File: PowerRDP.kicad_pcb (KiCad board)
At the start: 2 copper layers, 41.3 x 33.7 mm, 17 parts, among them J1 Conn_01x02_Male, J2 Conn_01x02_Male, J3 Conn_01x02_Male, J4 Conn_01x02_Male, J5 Conn_01x02_Male, J6 Conn_01x02_Male, J7 Conn_01x02_Male, J8 Conn_01x02_Male, J9 Conn_01x03_Male, U1 DPBW06F, U2 KA378R12C, U3 AZ1117-3.3

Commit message: Add pole descriptions on bottom silkscreen of +/-15V output
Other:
- board text added: "+"
- board text added: "-"
- board text added: "G"
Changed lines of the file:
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@@
   (general
     (thickness 1.6)
-    (drawings 16)
+    (drawings 19)
     (tracks 36)
     (zones 0)
@@
     (34 B.Paste user)
     (35 F.Paste user)
-    (36 B.SilkS user hide)
+    (36 B.SilkS user)
     (37 F.SilkS user)
     (38 B.Mask user)
-    (39 F.Mask user hide)
+    (39 F.Mask user)
     (40 Dwgs.User user)
     (41 Cmts.User user)
@@
       (xy -0.000377 -2.299489) (xy 0.01309 -2.299294)) (layer F.SilkS) (width 0.01))
   )
+  (gr_text - (at 159.766 63.754) (layer B.SilkS)
+    (effects (font (size 1 1) (thickness 0.2)) (justify mirror))
+  )
+  (gr_text + (at 157.226 63.754) (layer B.SilkS)
+    (effects (font (size 1 1) (thickness 0.2)) (justify mirror))
+  )
+  (gr_text G (at 154.432 63.754) (layer B.SilkS)
+    (effects (font (size 1 1) (thickness 0.2)) (justify mirror))
+  )
   (dimension 10.795 (width 0.3) (layer Eco1.User)

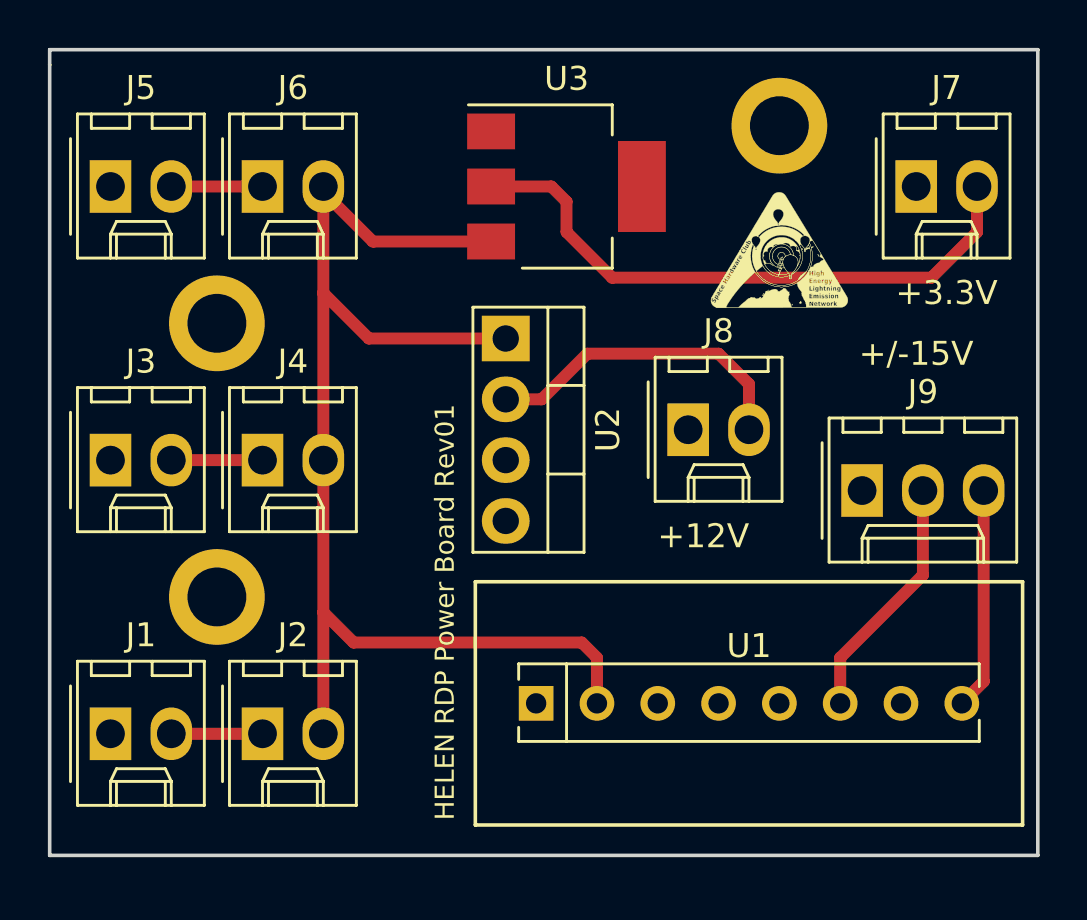
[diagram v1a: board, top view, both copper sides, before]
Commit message: Add power filtering to all regulators, correct +/-15V regulator
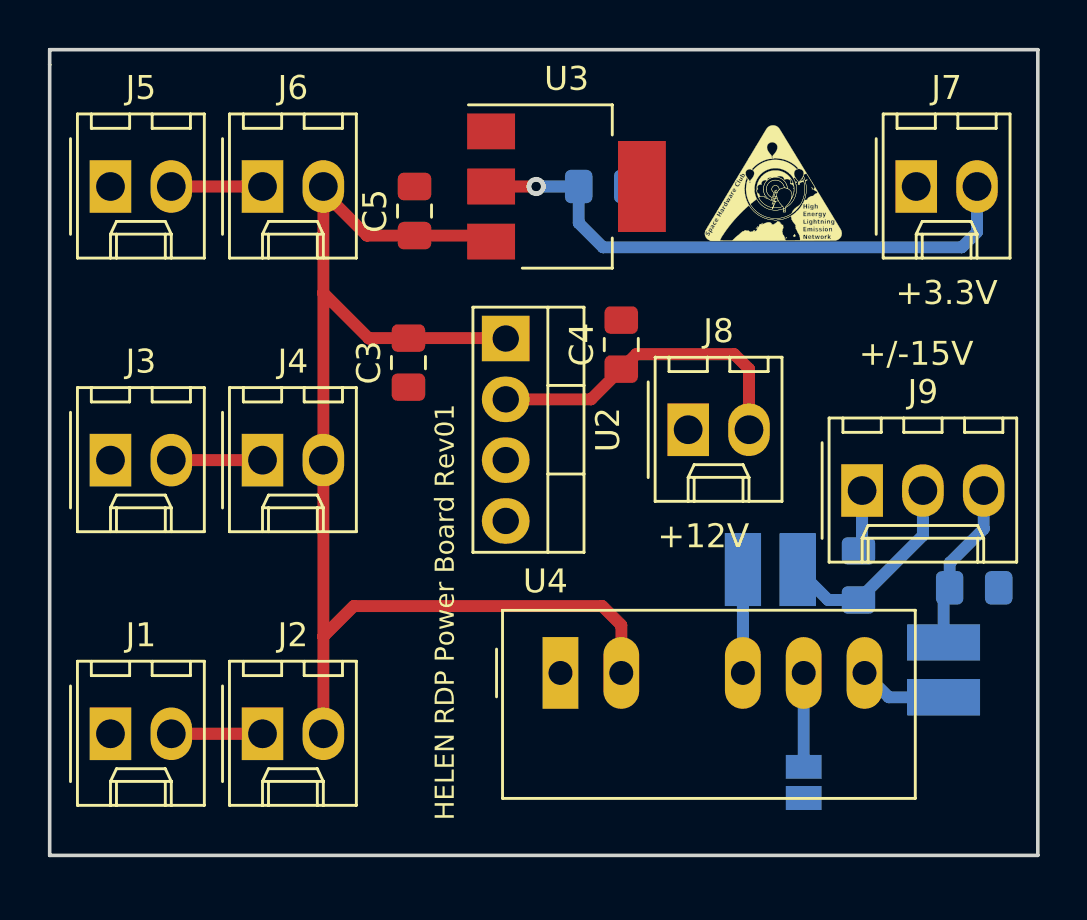
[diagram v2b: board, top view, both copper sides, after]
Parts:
- removed REF** (x3): ScrewHole, RDP-Power:ScrewHole
- removed U1: DPBW06F, RDP-Power:SIP-8_19x3mm_P2.54mm
- added C1: 1 uF, Capacitor_SMD:C_0805_2012Metric_Pad1.15x1.40mm_HandSolder, B.Cu at (154.4, 69.6)
- added C2: 1 uF, Capacitor_SMD:C_0805_2012Metric_Pad1.15x1.40mm_HandSolder, B.Cu at (159.3, 70.1)
- added C3: 10 uF, Capacitor_SMD:C_0805_2012Metric_Pad1.15x1.40mm_HandSolder, F.Cu at (135.6, 60.7)
- added C4: 47 uF, Capacitor_SMD:C_0805_2012Metric_Pad1.15x1.40mm_HandSolder, F.Cu at (144.5, 59.9)
- added C5: 10 uF, Capacitor_SMD:C_0805_2012Metric_Pad1.15x1.40mm_HandSolder, F.Cu at (135.9, 54.4)
- added C6: 22 uF, Capacitor_SMD:C_0805_2012Metric_Pad1.15x1.40mm_HandSolder, B.Cu at (143.8, 53.3)
- added JP1: Jumper, Jumper:SolderJumper-2_P1.3mm_Open_Pad1.0x1.5mm, B.Cu at (152.1, 78.2)
- added L1: 47 uH, RDP-Power:Murata 8200, B.Cu at (150.8, 69.3)
- added L2: 47 uH, RDP-Power:Murata 8200, B.Cu at (158.0, 73.5)
- added U4: TMR_1-1223, Converter_DCDC:Converter_DCDC_TRACO_TMR-1-xxxx_Dual_THT, F.Cu at (142.0, 73.7)
- U3: value AZ1117-3.3 -> AZ1117CH-3.3
- moved G*** 7.38 mm to (135.6, 62.7), turned to 0 degrees
- moved G*** 2.81 mm to (150.9, 53.1)
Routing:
- net Net-(L1-Pad1): track 0.00 -> 4.32 mm
- net Net-(JP1-Pad1): track 0.00 -> 3.92 mm
- net Net-(L2-Pad1): track 0.00 -> 3.72 mm
- net GND: track 0.00 -> 2.59 mm
- net /-15V: track 9.27 -> 7.04 mm
- net /+15V: track 10.3 -> 8.75 mm
- net +BATT: track 76.4 -> 77.5 mm
- net /+3.3V: track 25.3 -> 24.4 mm, vias 0 -> 1

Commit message: Re-add drill holes
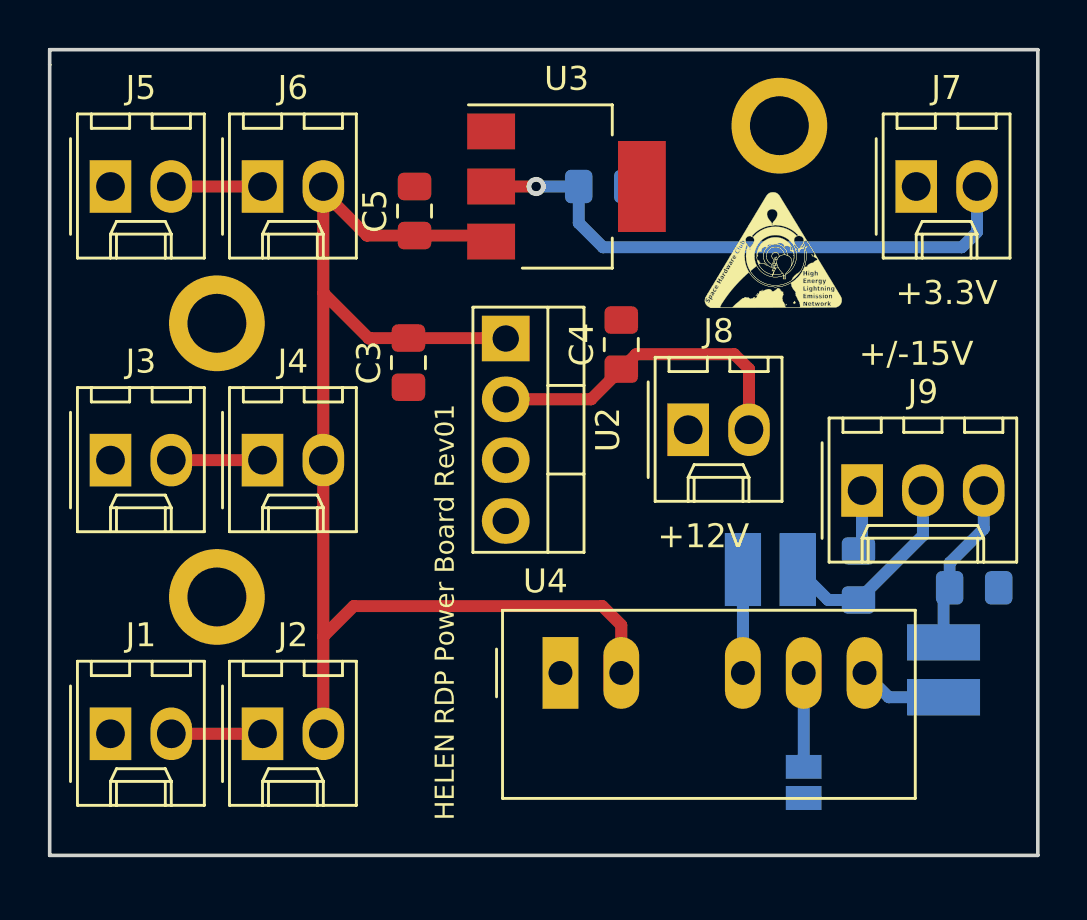
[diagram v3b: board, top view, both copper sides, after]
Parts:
- added REF**: ScrewHole, rdplibs:ScrewHole, F.Cu at (151.1, 50.8)
- added REF**: ScrewHole, rdplibs:ScrewHole, F.Cu at (127.6, 70.5)
- added REF**: ScrewHole, rdplibs:ScrewHole, F.Cu at (127.6, 59.1)
- moved G*** 2.79 mm to (150.9, 55.9)
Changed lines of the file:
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@@
     (tracks 54)
     (zones 0)
-    (modules 23)
+    (modules 26)
     (nets 14)
   )
@@
   )
   (setup
-    (last_trace_width 0.5)
+    (last_trace_width 0.25)
     (user_trace_width 0.5)
     (user_trace_width 1)
@@
   )
   (module RDP-Power:HELENlogo (layer F.Cu)
-    (at 150.876 53.086)
+    (at 150.876 55.88)
     (fp_text reference G*** (at 0 0) (layer F.SilkS) hide
       (effects (font (size 1.524 1.524) (thickness 0.3)))
@@
       (xy 14.151064 -15.106562)) (layer B.SilkS) (width 0.01))
   )
+  (module rdplibs:ScrewHole (layer F.Cu)
+    (at 151.13 50.8)
+    (descr "Single banana socket, footprint - 6mm drill")
+    (tags "banana socket")
+    (fp_text reference REF** (at 0 -6.5) (layer F.SilkS) hide
+      (effects (font (size 1 1) (thickness 0.15)))
+    )
+    (fp_text value ScrewHole (at -0.25 6.5) (layer F.Fab)
+      (effects (font (size 1 1) (thickness 0.15)))
+    )
+    (fp_text user %R (at 0 0) (layer F.Fab)
+      (effects (font (size 0.8 0.8) (thickness 0.12)))
+    )
+    (fp_circle (center 0 0) (end 2 0) (layer F.Fab) (width 0.1))
+    (pad "" np_thru_hole circle (at 0 0) (size 4 4) (drill 2.46) (layers *.Cu *.Mask))
+    (model ${KISYS3DMOD}/Connector.3dshapes/Banana_Jack_1Pin.wrl
+      (at (xyz 0 0 0))
+      (scale (xyz 2 2 2))
+      (rotate (xyz 0 0 0))
+    )
+  )
+  (module rdplibs:ScrewHole (layer F.Cu)
+    (at 127.635 70.485)
+    (descr "Single banana socket, footprint - 6mm drill")
+    (tags "banana socket")
+    (fp_text reference REF** (at 0 -6.5) (layer F.SilkS) hide
+      (effects (font (size 1 1) (thickness 0.15)))
+    )
+    (fp_text value ScrewHole (at -0.25 6.5) (layer F.Fab)
+      (effects (font (size 1 1) (thickness 0.15)))
+    )
+    (fp_text user %R (at 0 0) (layer F.Fab)
+      (effects (font (size 0.8 0.8) (thickness 0.12)))
+    )
+    (fp_circle (center 0 0) (end 2 0) (layer F.Fab) (width 0.1))
+    (pad "" np_thru_hole circle (at 0 0) (size 4 4) (drill 2.46) (layers *.Cu *.Mask))
+    (model ${KISYS3DMOD}/Connector.3dshapes/Banana_Jack_1Pin.wrl
+      (at (xyz 0 0 0))
+      (scale (xyz 2 2 2))
+      (rotate (xyz 0 0 0))
+    )
+  )
+  (module rdplibs:ScrewHole (layer F.Cu)
+    (at 127.635 59.055)
+    (descr "Single banana socket, footprint - 6mm drill")
+    (tags "banana socket")
+    (fp_text reference REF** (at 0 -6.5) (layer F.SilkS) hide
+      (effects (font (size 1 1) (thickness 0.15)))
+    )
+    (fp_text value ScrewHole (at -0.25 6.5) (layer F.Fab)
+      (effects (font (size 1 1) (thickness 0.15)))
+    )
+    (fp_text user %R (at 0 0) (layer F.Fab)
+      (effects (font (size 0.8 0.8) (thickness 0.12)))
+    )
+    (fp_circle (center 0 0) (end 2 0) (layer F.Fab) (width 0.1))
+    (pad "" np_thru_hole circle (at 0 0) (size 4 4) (drill 2.46) (layers *.Cu *.Mask))
+    (model ${KISYS3DMOD}/Connector.3dshapes/Banana_Jack_1Pin.wrl
+      (at (xyz 0 0 0))
+      (scale (xyz 2 2 2))
+      (rotate (xyz 0 0 0))
+    )
+  )
   (gr_text - (at 159.766 63.754) (layer B.SilkS)
